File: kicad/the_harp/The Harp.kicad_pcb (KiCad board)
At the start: 4 copper layers, 56 x 94.5 mm, 181 parts, among them IC501 AK4621EF, J401 PJ-063AH, J402 NMJ6HCD2, J403 NMJ6HCD2, J404 NMJ6HCD2, J405 Bypass FSW, J406 NMJ6HCD2, J407 Hold FSW, J408 OLED 0.91 128x32, K401 G6K-2F-Y, Q401 2N7002, Q402 2N7002, Q403 2N7002, SW101 100-DP6, SW102 100-DP6, SW103 100-DP6, U201 STM32H750VBT6, U202 W25Q128JVSIQ, U301 TPS54202DDC, U302 NCP718ASN500T1G, U401 MCP6001T-I/OT, U501 OPA2348AIDR, U601 THS4522IPW, U701 OPA2365AIDR, U702 OPA1688IDR, Y201 25MHz 9pF

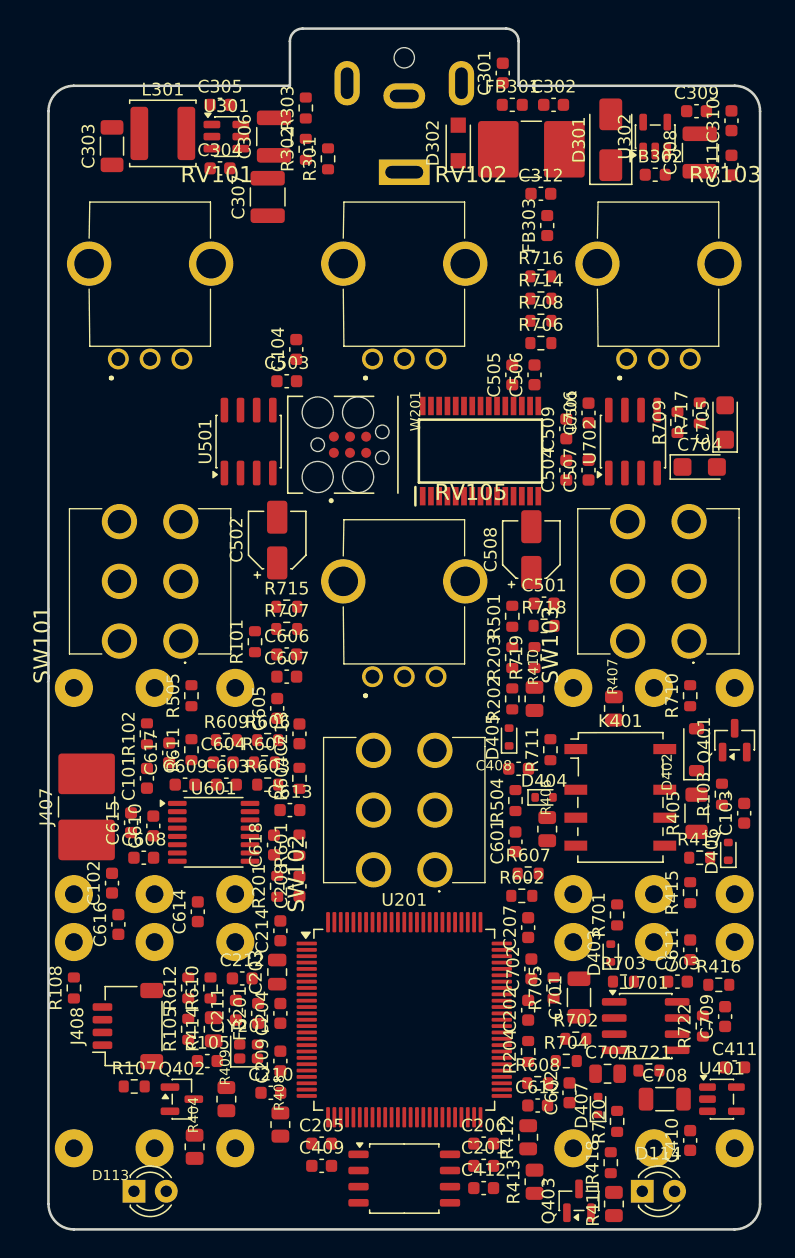
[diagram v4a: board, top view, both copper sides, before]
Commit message: Two-sided placement: fix the three weak spots
37 parts that gain nothing from the top move to the bottom, where the jack
bodies leave room (above the upper jacks, the centre strip, the heel
strip): the relay and its driver under U201, the LED and footswitch
drivers, the expression buffer, the pot RC filters, and the SWD and
footswitch pads (bare copper). That frees the middle of the top:
- codec next to the MCU's SAI pins: SAI 50-55 mm -> 15-17 mm
- ADC driver next to the input buffers, feedback networks compact
  (worst 39 -> 18 mm), anti-alias caps at the codec's input pins
- input path: IN 35 -> 28 mm, relay to buffer 22 -> 11 mm
Remaining long run: the driven ADC pair to the codec (~30 mm between parts).

Placer and writer handle both sides (flip as KiCad does: local Y
mirrored, angles negated, layers swapped, text mirrored); verify.py
re-reads the file and checks both sides and every pad position. IC501
gets the courtyard its footprint lacked. Docs, report and drawings updated;
bottom-side parts need double-sided assembly or hand fitting.

Co-Authored-By: Claude Opus 5.5 <noreply@anthropic.com>
Claude-Session: https://claude.ai/code/session_016hDejPHPgG8auBLMyByYZK
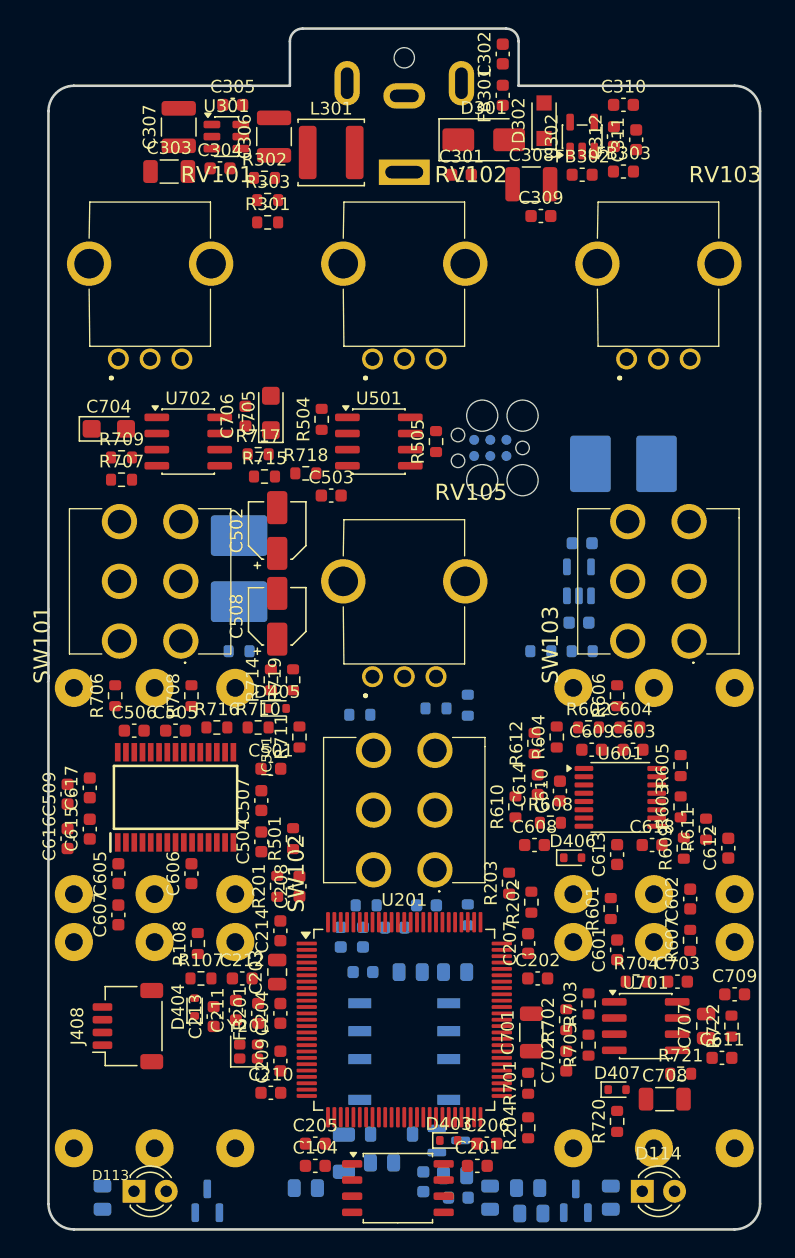
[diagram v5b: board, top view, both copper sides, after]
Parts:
- C101, C102, C103, C105, C408, C409, C410, C411, C412, D402, J405, J407, K401, Q401, Q402, Q403, R101, R102, R103, R105, R404, R405, R406, R407, R408, R409, R410, R411, R412, R413, R414, R415, R416, R417, R418, U401, W201: moved to B.Cu
- moved C104 64.3 mm to (141.5, 138.0), turned to 0 degrees
- moved J407 50.1 mm to (165.8, 82.8), turned to 0 degrees
- moved C509 48.7 mm to (122.0, 108.8)
- moved C704 46.6 mm to (125.2, 80.0)
- moved R709 43.8 mm to (126.2, 82.2), turned to 0 degrees
- moved R716 43.7 mm to (133.8, 103.5)
- moved R706 43.5 mm to (125.8, 101.0), turned to 90 degrees
- moved C411 43.0 mm to (162.5, 89.0)
- moved U401 42.3 mm to (162.2, 92.0), turned to 90 degrees
- moved C506 42.1 mm to (127.2, 103.8), turned to 0 degrees
- moved C410 41.7 mm to (162.2, 95.2), turned to 0 degrees
- moved R611 41.0 mm to (172.2, 111.5)
- moved R708 40.3 mm to (131.8, 101.0), turned to 90 degrees
- moved J405 40.2 mm to (135.5, 91.0), turned to 90 degrees
- moved Q401 38.7 mm to (152.0, 136.0), turned to 0 degrees
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
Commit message: Option 1: OLED at (0, -5), Retune toggle at (0, -24), re-placed board
Face: the OLED window moves up into the middle of the face under the
Jawari knob, the Retune toggle moves down to (0, -24) (design brief,
decision 16). The module is mounted turned round, pads at its right end;
the firmware flips the image.

Board: with the toggle out of the middle the H750 moves up to (0, -7),
under the screen. Codec beside it next to the SAI pins (11-16 mm), ADC
driver below the codec (left ADC pair 17-19 mm), input buffers and flash
on the right next to IN, output stages and VCOM buffers between the pot
rows, J408 at the module's right end (22, -3.5). Bottom side as before,
relay now under U201 at (0, -8). Placer now works on a 0.5 mm grid and
prefers spots that line up with the rest of the group and share its
orientation. Checked from the board file: no overlaps either side,
nothing on through-holes, nothing tall under the module.

Face cut-out and OLED drawings, placement drawing, PCB plan, brief,
firmware requirements, design report and schematic notes updated.

Co-Authored-By: Claude Opus 5.5 <noreply@anthropic.com>
Claude-Session: https://claude.ai/code/session_016hDejPHPgG8auBLMyByYZK
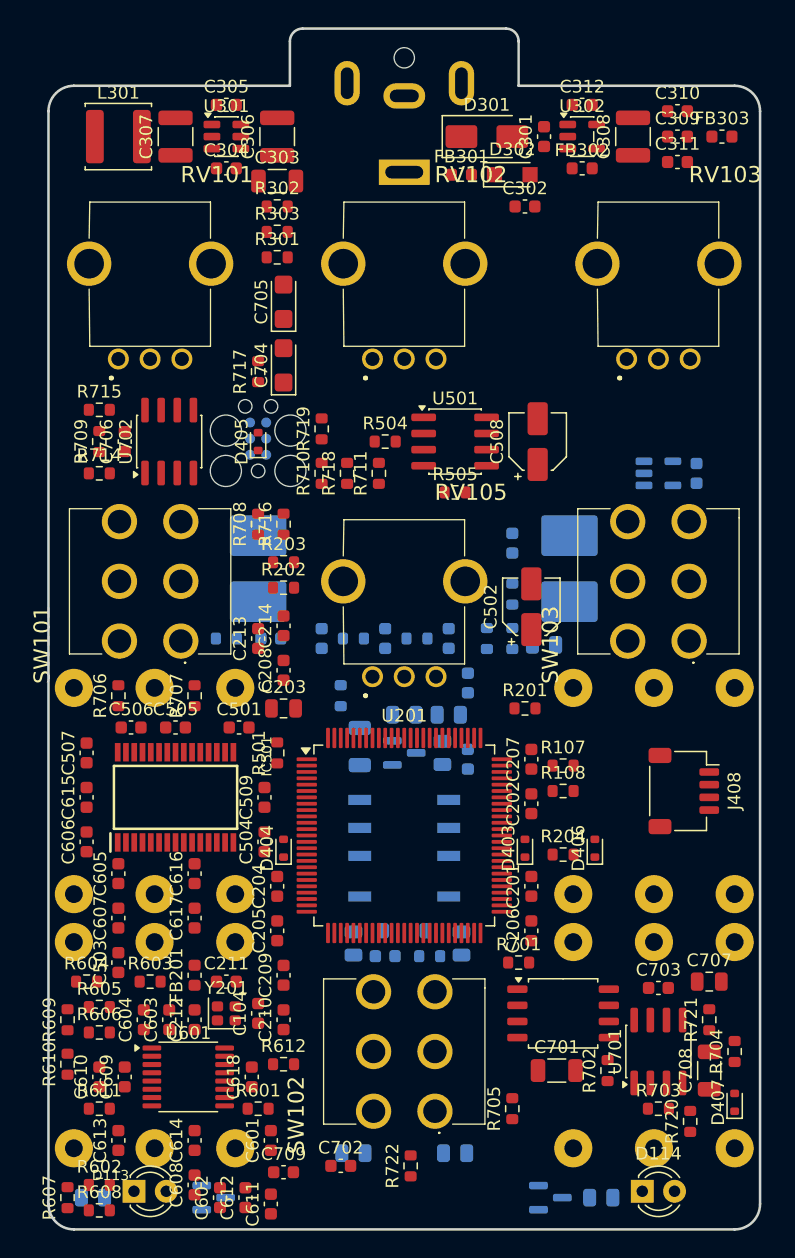
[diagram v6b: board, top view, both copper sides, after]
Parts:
- moved R607 53.0 mm to (122.0, 140.5)
- moved R602 52.7 mm to (124.5, 139.5)
- moved R611 52.6 mm to (124.5, 133.5), turned to 0 degrees
- moved R609 50.3 mm to (122.0, 126.5)
- moved R605 49.5 mm to (124.5, 125.5), turned to 0 degrees
- moved R606 48.6 mm to (124.5, 127.5), turned to 0 degrees
- moved J408 47.5 mm to (170.5, 108.5), turned to 270 degrees
- moved C612 46.9 mm to (136.0, 140.5)
- moved R608 46.8 mm to (124.5, 141.5)
- moved C613 45.2 mm to (126.0, 136.0)
- moved C609 44.9 mm to (126.5, 131.0), turned to 90 degrees
- moved C604 44.6 mm to (128.0, 126.5), turned to 90 degrees
- moved R603 44.0 mm to (128.5, 123.5), turned to 0 degrees
- moved C602 43.8 mm to (134.0, 140.5)
- moved R414 43.7 mm to (159.5, 97.0), turned to 0 degrees
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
